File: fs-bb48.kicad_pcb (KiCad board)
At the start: 2 copper layers, 35 x 12.1 mm, 20 parts, among them P1 USB, P2 SWD, P3 PWR, P4 EXT, T1 TOUCH_PAD, U1 MKL27Z256VFM4, U2 NUP2114

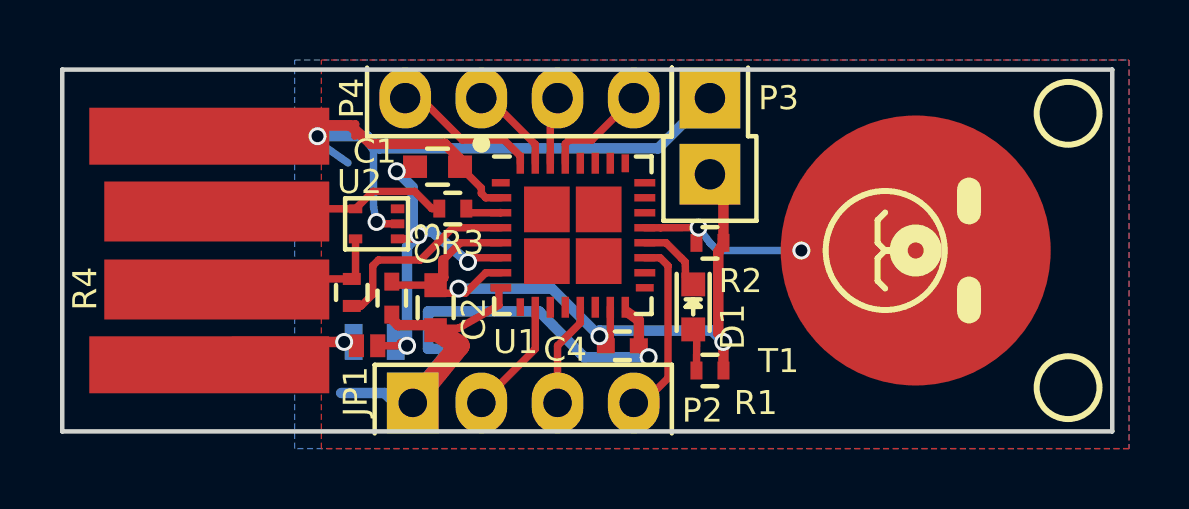
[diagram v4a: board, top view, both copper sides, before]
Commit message: Remove C3, fix FB1, add hole, fix solder paste of U1
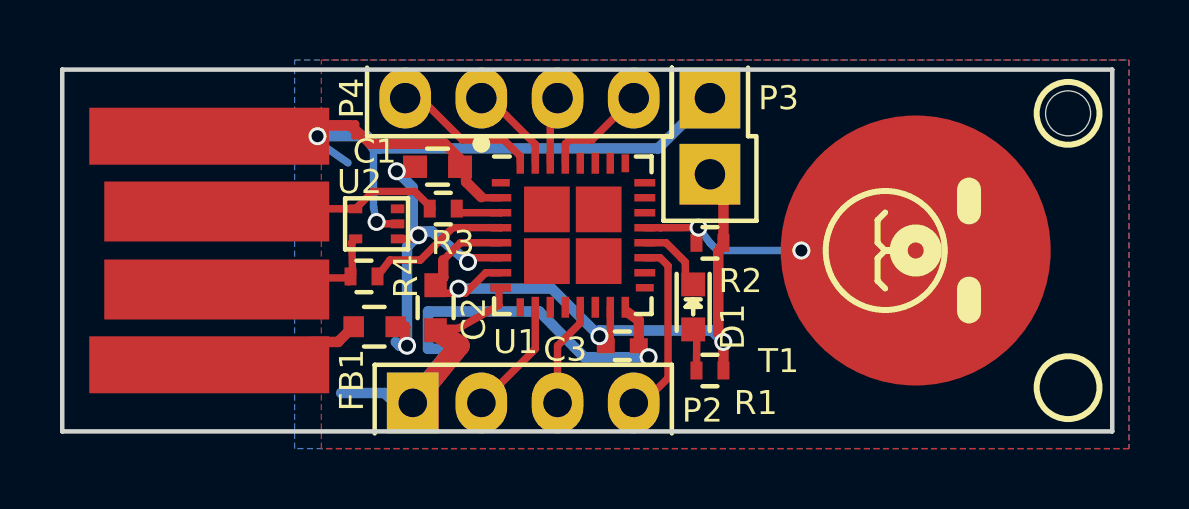
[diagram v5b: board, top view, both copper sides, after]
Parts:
- removed the C3 at (137.5, 108.5)
- removed JP1: Jumper_NC_Small, fs-bb48:SOLDER_JUMPER
- added H1: Hole, fs-bb48:Hole, F.Cu at (160.0, 102.4)
- FB1: footprint fs-bb48:Inductor_SM0603 -> fs-bb48:FB_SM0603; moved to F.Cu
- FST-LOGO: value VAL** -> LOGO1
- moved R4 0.67 mm to (136.6, 107.8), turned to 180 degrees
- moved FB1 0.51 mm to (136.9, 109.5)
- moved R3 0.32 mm to (139.2, 105.5)
- renumbered C4 to C3
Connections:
- U1 pad 1: (no net) -> Net-(U1-Pad1)
- U2 pad 3: (no net) -> Net-(U2-Pad3)
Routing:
- net /VBUS_: track 5.70 -> 7.52 mm, vias 1 -> 0
- net /D-: track 6.60 -> 4.83 mm
- net GND: track 65.5 -> 63.9 mm
- net +3V3: track 29.5 -> 28.0 mm
- net /D-_: track 6.04 -> 6.65 mm

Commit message: modify VBUS line
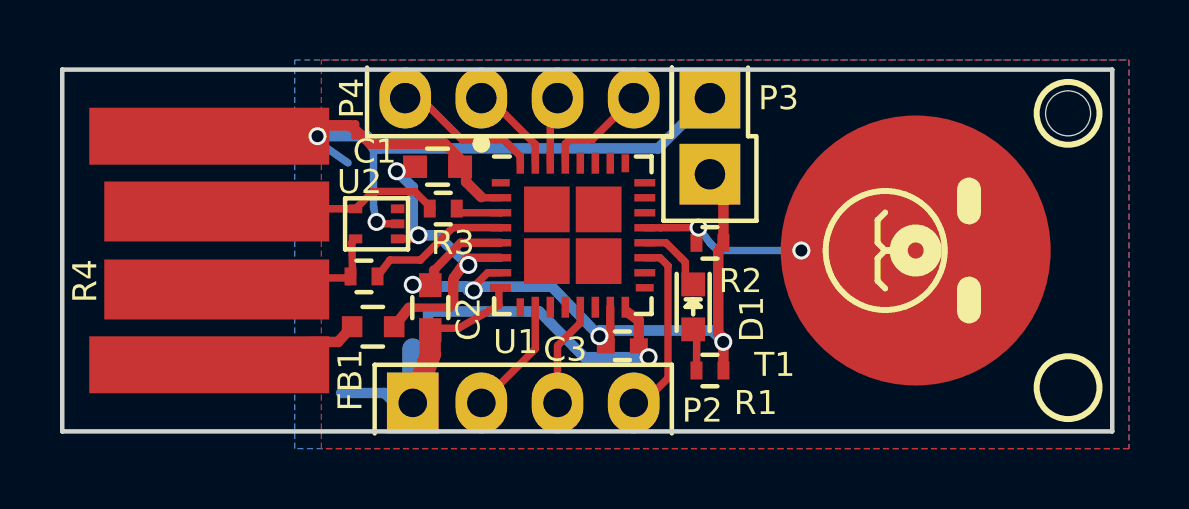
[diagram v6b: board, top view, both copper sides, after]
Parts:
- moved C2 0.18 mm to (138.8, 108.8)
- moved FB1 0.05 mm to (136.9, 109.5)
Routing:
- net /VBUS: track 14.6 -> 11.3 mm, vias 4 -> 3
- net +3V3: track 28.0 -> 31.2 mm, vias 3 -> 4
- net GND: track 63.9 -> 61.5 mm
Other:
- net class 3V3 added: clearance 0.2, trace_width 0.282, via_dia 0.6, via_drill 0.4
